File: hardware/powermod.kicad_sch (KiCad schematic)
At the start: 74 parts, among them J1 USB_C_IN, J2 USB_C_OUT, J3 JST_PH_2, J4 STEMMA_QT, J5 SWD_HDR, Q1 AON7407, Q2 AON7407, Q3 BSS138, SW1 BUTTON, U1 BM8563ESA, U2 PY32F003F18P6, U3 TPS63020DSJR, U4 TP4056, U5 XC6206P332MR, Y1 Q13FC13500004

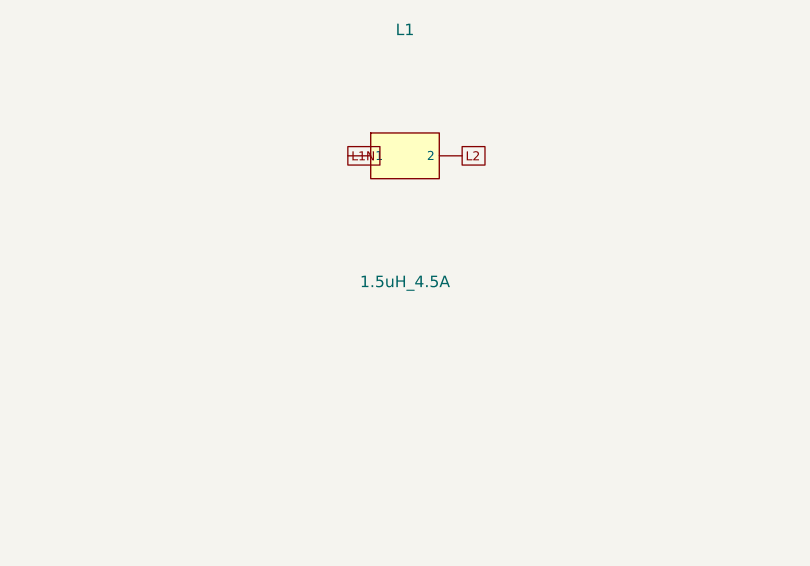
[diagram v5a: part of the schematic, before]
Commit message: hardware: in-stock swaps for L1 inductor + SW1 button (LCSC-only, no re-layout)
- L1: Sumida CDMC6D28 (OOS) -> CYA0650-1.5UH (C5189751, ~11k). Lands are
  2.35x3.5mm @ 5.7mm pitch = same pitch as the existing L_Sumida_CDMC6D28
  footprint, body 7.2x6.6mm ~ same, so it drops onto the current land pattern
  with no board change. Confirm exact Isat/Irms on datasheet (size implies ~9A).
- SW1: C&K PTS647SK50 (OOS) -> PTS647SN50 (C2799414, ~9k). Same PTS647 4.5x4.5
  SMD footprint; N vs K is only plunger height. Drop-in.

Whole BOM now in-stock except J5 (SWD hand-solder header, DNP by design). The
only board change for the all-in-stock goal is the MCU (TSSOP-20), already done.

Co-Authored-By: Claude Opus 4.8 <noreply@anthropic.com>
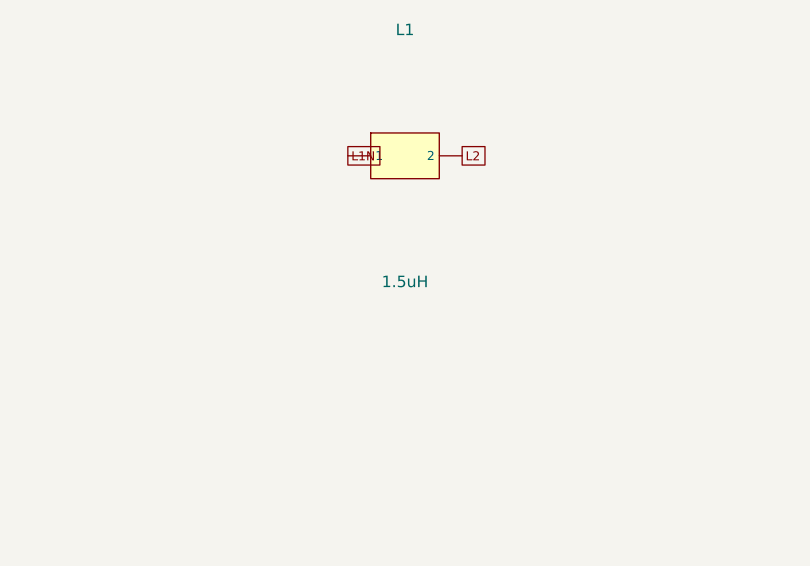
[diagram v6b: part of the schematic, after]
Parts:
- L1: value 1.5uH_4.5A -> 1.5uH
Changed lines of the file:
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@@
  (symbol (lib_id "powermod:PM_L1") (at 314.96000000000004 30.48 0) (unit 1) (in_bom yes) (on_board yes)
   (property "Reference" "L1" (at 314.96000000000004 16.48 0) (effects (font (size 1.27 1.27))))
-  (property "Value" "1.5uH_4.5A" (at 314.96000000000004 44.480000000000004 0) (effects (font (size 1.27 1.27))))
+  (property "Value" "1.5uH" (at 314.96000000000004 44.480000000000004 0) (effects (font (size 1.27 1.27))))
   (property "Footprint" "Inductor_SMD:L_Sumida_CDMC6D28_7.25x6.5mm" (at 314.96000000000004 30.48 0) (effects (font (size 1.27 1.27)) hide))
   (pin "1")

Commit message: hardware: J5 3-pin+TP7 -> 4-pin SWD header (NRST folded in) [WIP]
Fold the NRST probe pad (TP7) into J5 as a 4th header pin: J5 1x03 -> 1x04
(GND/SWCLK/SWDIO/NRST), TP7 removed, NRST net now U2.18 + J5.4. Cleaner
programming connector (proper connect-under-reset pin, no loose test pad).

WIP: J5's default in-place spot puts pin 4 over routed copper (a GND stitch via
+ VOUT/3V3 traces). User repositions J5 to a clear area next; then reroute its
4 connections + refill + DRC + regen CPL/gerbers. pad-diff 226/226.

Co-Authored-By: Claude Opus 4.8 <noreply@anthropic.com>
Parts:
- removed TP7: NRST_PAD, TestPoint:TestPoint_Pad_2.0x2.0mm, symbol powermod:PM_TP7
- J5: footprint Connector_PinHeader_2.54mm:PinHeader_1x03_P2.54mm_Vertical -> Connector_PinHeader_2.54mm:PinHeader_1x04_P2.54mm_Vertical
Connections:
- net NRST: now also J5.4 (NRST)
